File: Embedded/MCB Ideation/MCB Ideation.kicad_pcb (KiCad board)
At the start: 2 copper layers, 19.2 x 26.6 mm, 21 parts, among them J1 USB, J2 Power, J3 MicroSD, U1 Sensored, U2 Expansion, U3 Comms Link Expansion, U4 AP7366-33W5-7

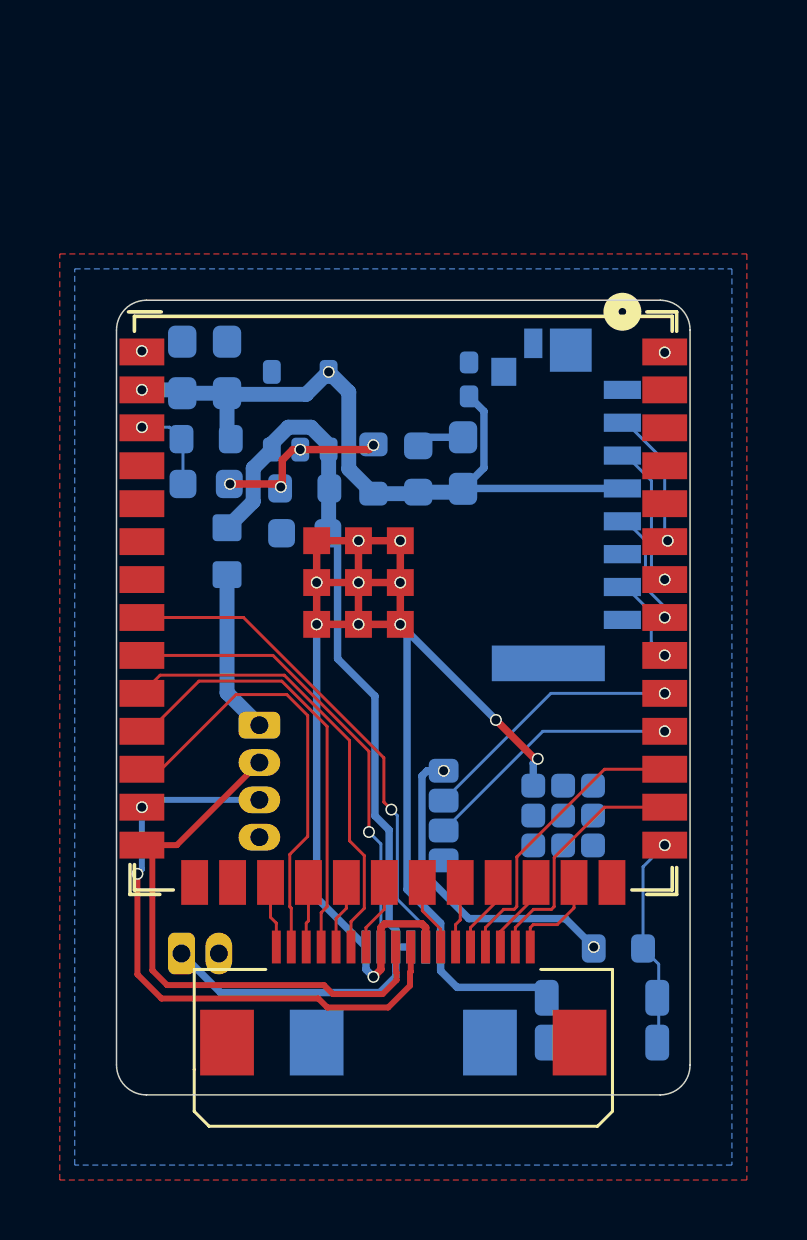
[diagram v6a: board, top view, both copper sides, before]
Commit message: Modified GPIO Expansion Pins
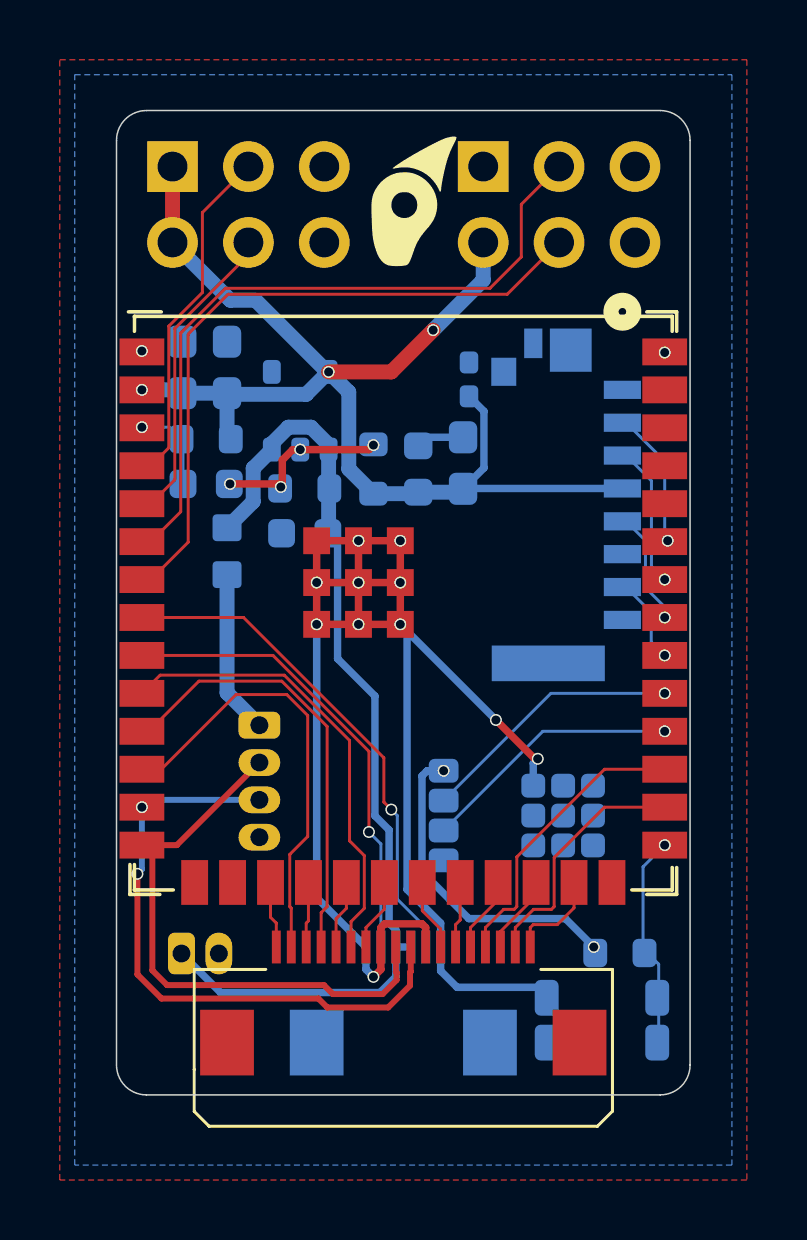
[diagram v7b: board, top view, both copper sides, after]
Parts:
- added J4: GPIO Pair 0, Connector_PinHeader_2.54mm:PinHeader_2x03_P2.54mm_Vertical, B.Cu at (132.3, 85.1)
- added J5: GPIO Pair 1, Connector_PinHeader_2.54mm:PinHeader_2x03_P2.54mm_Vertical, B.Cu at (142.7, 85.1)
- added REF**: Logo_5mm, Logo:Logo_5mm, F.Cu at (140.1, 86.3)
- moved R2 0.16 mm to (147.2, 111.4)
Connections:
- ESP1 pad 4: unconnected-(ESP1-GPIO4/TOUCH4/ADC1_CH3-Pad4) -> GPIO 0
- ESP1 pad 5: unconnected-(ESP1-GPIO5/TOUCH5/ADC1_CH4-Pad5) -> GPIO 1
- ESP1 pad 6: unconnected-(ESP1-GPIO6/TOUCH6/ADC1_CH5-Pad6) -> GPIO 2
- ESP1 pad 7: unconnected-(ESP1-GPIO7/TOUCH7/ADC1_CH6-Pad7) -> GPIO 3
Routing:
- net GPIO 2: track 0.00 -> 23.7 mm
- net GPIO 3: track 0.00 -> 22.7 mm
- net +3V3: track 35.7 -> 53.0 mm, vias 4 -> 5
- net GPIO 0: track 0.00 -> 11.7 mm
- net GPIO 1: track 0.00 -> 10.4 mm
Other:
- board size 19.2 x 26.6 mm -> 19.2 x 33 mm
- board text added: "3V3"
- board text added: "5 4"
- board text added: "7 6"
- board text added: "GND"
